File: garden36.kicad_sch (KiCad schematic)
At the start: 82 parts, among them J1 Conn_01x02, J2 Conn_01x02, SW1 SW_SPDT, SW2 SW_Push, SW3 SW_SPDT, SW4 SW_Push, U1 nice_nano, U2 nice_nano

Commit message: Update libraries continue with updates for project
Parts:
- removed J1, J2: Conn_01x02, Connector_JST:JST_PH_S2B-PH-K_1x02_P2.00mm_Horizontal, symbol Connector_Generic:Conn_01x02
- SW2, SW4: footprint Button_Switch_SMD:SW_SPST_TL3305A -> Button_Switch_SMD:SW_SPST_B3U-1000P
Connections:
- net B+: no longer names the net of U1.29 (BAT+)
- net B-: no longer names the net of U1.28 (GND)
- net R_B+: no longer names the net of U2.29 (BAT+)
- net R_B-: no longer names the net of U2.28 (GND)
- no-connect marks 2 -> 6

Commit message: Switches set
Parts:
- added PW1, PW4: ~, garden:Battery, symbol kometa:Battery
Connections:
- net GND: now also PW1.2 (BAT-)
- net R_GND: now also PW4.2 (BAT-)
- net BAT: no longer names the net of SW1.2 (B)
- net BAT: now also PW1.1 (BAT+)
- net R_BAT: no longer names the net of SW3.2 (B)
- net R_BAT: now also PW4.1 (BAT+)
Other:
- moved on the sheet: SW1, SW3

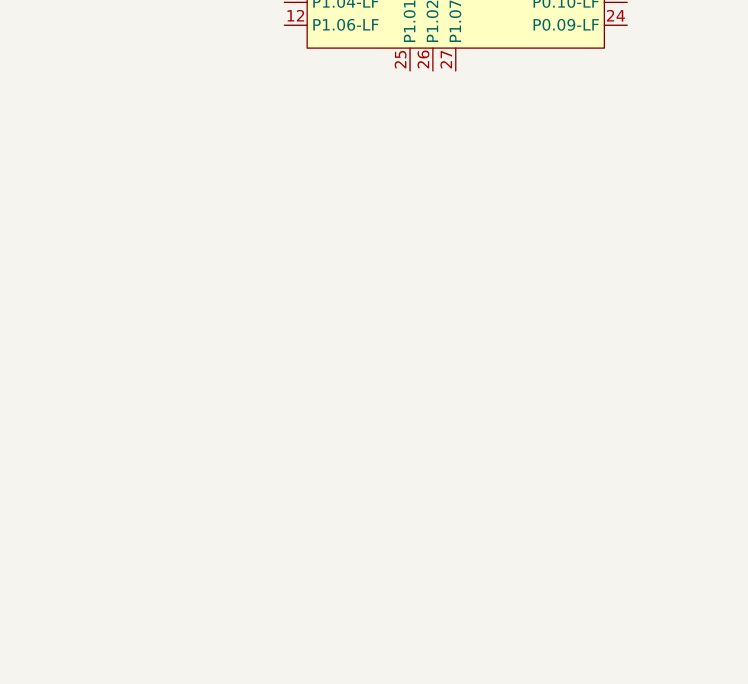
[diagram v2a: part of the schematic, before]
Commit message: Mounting holes for left added
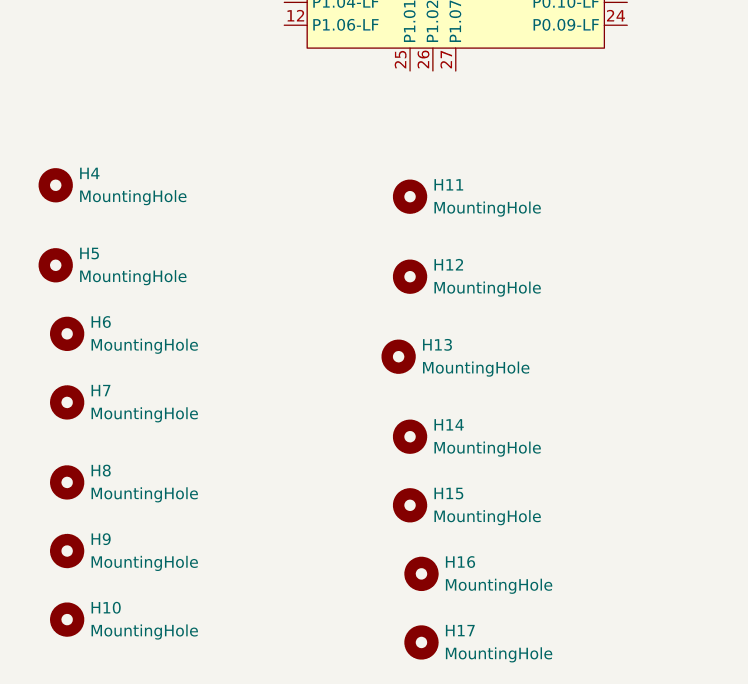
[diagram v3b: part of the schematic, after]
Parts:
- added H10, H11, H12, H13, H14, H15, H16, H17, H4, H5, H6, H7, H8, H9: MountingHole, MountingHole:MountingHole_2.2mm_M2, symbol Mechanical:MountingHole

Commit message: Start adding routes
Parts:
- added MB4, MB5: ~, PCM_marbastlib-various:mousebites_1mm, symbol garden:MouseBites
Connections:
- net COL0: now also U1.7 (P0.22)
- net COL1: now also U1.8 (P0.24)
- net COL2: now also U1.18 (P0.29-LF)
- net COL3: now also U1.19 (P0.02-LF)
- net COL4: now also U1.20 (P1.15-LF)
- net ROW0: now also U1.21 (P1.13-LF)
- net ROW1: now also U1.22 (P1.11-LF)
- net ROW2: now also U1.23 (P0.10-LF)
- net ROW3: now also U1.24 (P0.09-LF)
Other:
- moved on the sheet: H11, H12, H13, H14, H15, H16, H17
